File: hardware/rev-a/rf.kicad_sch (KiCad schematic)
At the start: 20 parts, among them J5 U.FL

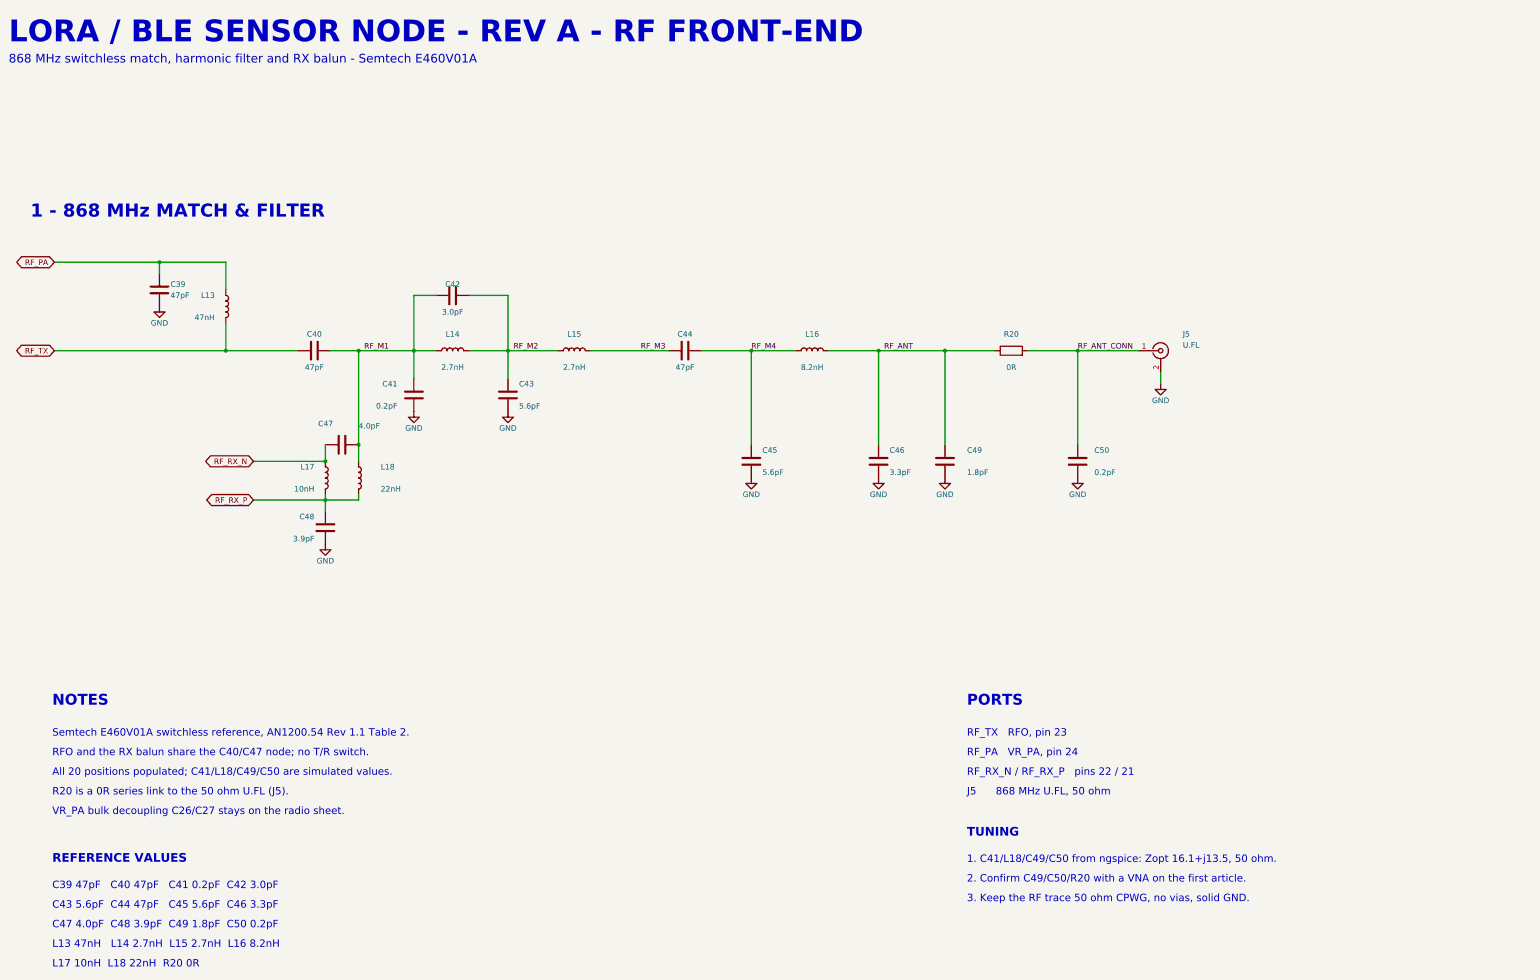
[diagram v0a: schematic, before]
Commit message: Schematic: cosmetic pass over the sheet artwork
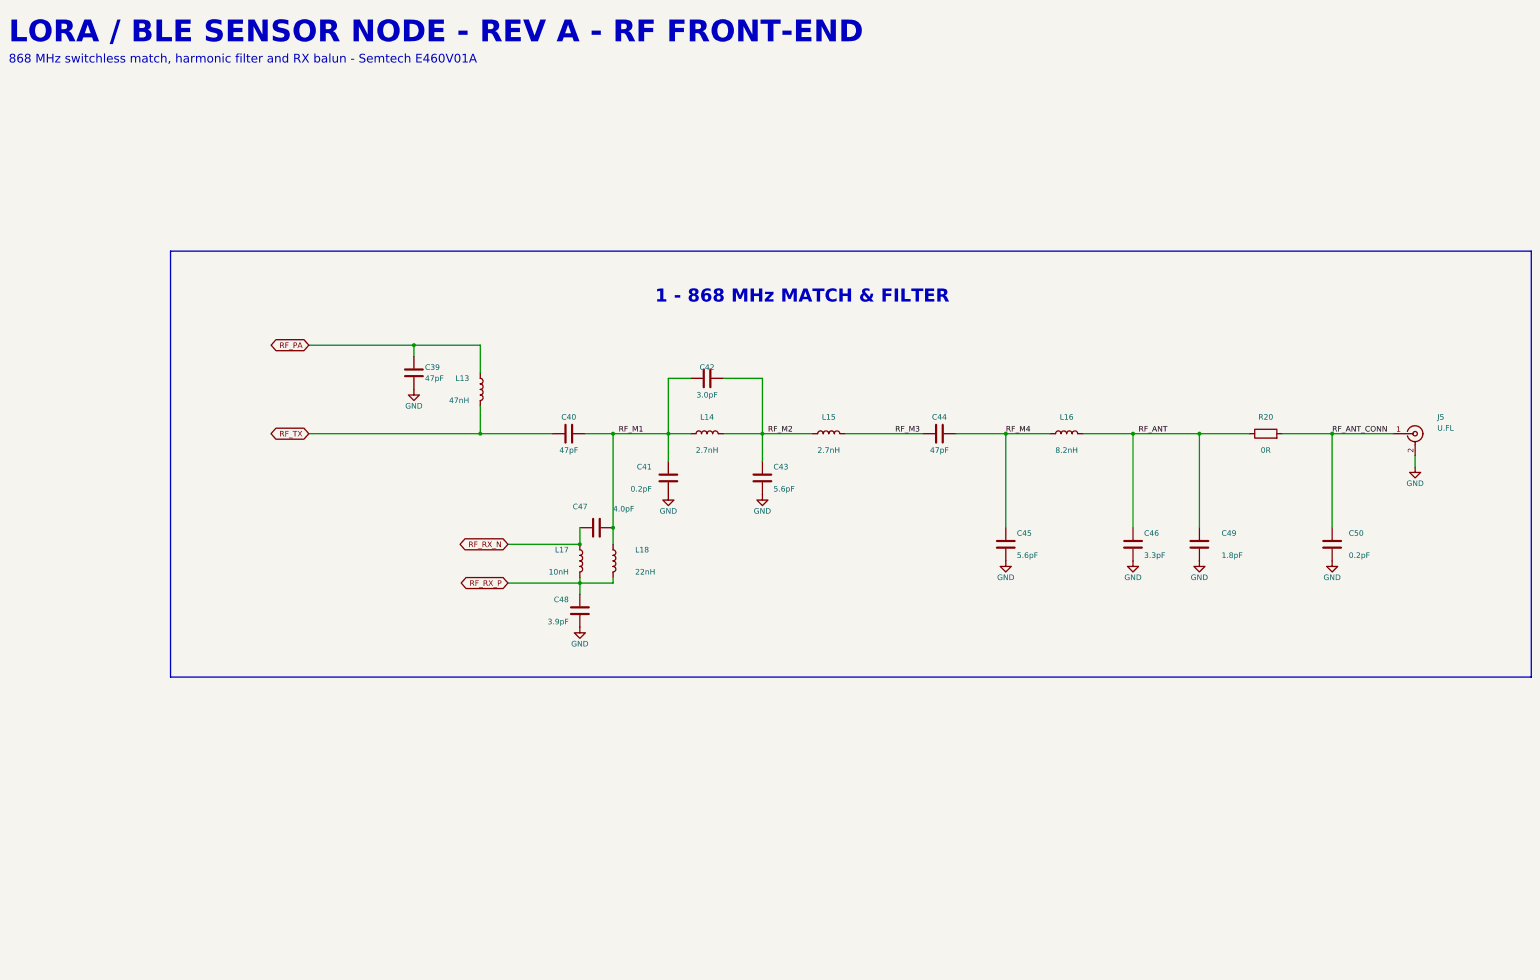
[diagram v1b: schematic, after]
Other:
- note removed: "1. C41/L18/C49/C50 from ngspice: Zopt 16.1+j13.5, 50 ohm."
- note removed: "2. Confirm C49/C50/R20 with a VNA on the first article."
- note removed: "3. Keep the RF trace 50 ohm CPWG, no vias, solid GND."
- note removed: "All 20 positions populated; C41/L18/C49/C50 are simulated values."
- note removed: "C39 47pF C40 47pF C41 0.2pF C42 3.0pF"
- note removed: "C43 5.6pF C44 47pF C45 5.6pF C46 3.3pF"
- note removed: "C47 4.0pF C48 3.9pF C49 1.8pF C50 0.2pF"
- note removed: "J5 868 MHz U.FL, 50 ohm"
- note removed: "L13 47nH L14 2.7nH L15 2.7nH L16 8.2nH"
- note removed: "L17 10nH L18 22nH R20 0R"
- note removed: "NOTES"
- note removed: "PORTS"
- note removed: "R20 is a 0R series link to the 50 ohm U.FL (J5)."
- note removed: "REFERENCE VALUES"
- note removed: "RFO and the RX balun share the C40/C47 node; no T/R switch."
- note removed: "RF_PA VR_PA, pin 24"
- note removed: "RF_RX_N / RF_RX_P pins 22 / 21"
- note removed: "RF_TX RFO, pin 23"
- note removed: "Semtech E460V01A switchless reference, AN1200.54 Rev 1.1 Table 2."
- note removed: "TUNING"
- note removed: "VR_PA bulk decoupling C26/C27 stays on the radio sheet."
- moved on the sheet: C39, C40, C41, C42, C43, C44, C45, C46, C47, C48, C49, C50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
